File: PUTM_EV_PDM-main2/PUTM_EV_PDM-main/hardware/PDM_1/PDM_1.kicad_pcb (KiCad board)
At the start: 4 copper layers, 55 x 100 mm, 148 parts, among them IC2 BTS722204ESAXUMA1, IC3 BTS722204ESAXUMA1, IC4 BTS722204ESAXUMA1, IC5 BTS722204ESAXUMA1, J1 FTSH-107-01-L-DV-K-A, J2 UPT-08-01-01-L-RA, J5 UPT-02-01-01-X-RA, J6 Conn_01x06, J7 UPT-08-01-01-L-RA, U1 STM32G0C1KCTxN, U2 LD1117S33TR_SOT223, U3 LM2675M-5.0/NOPB, U5 MCP2542FDxMF

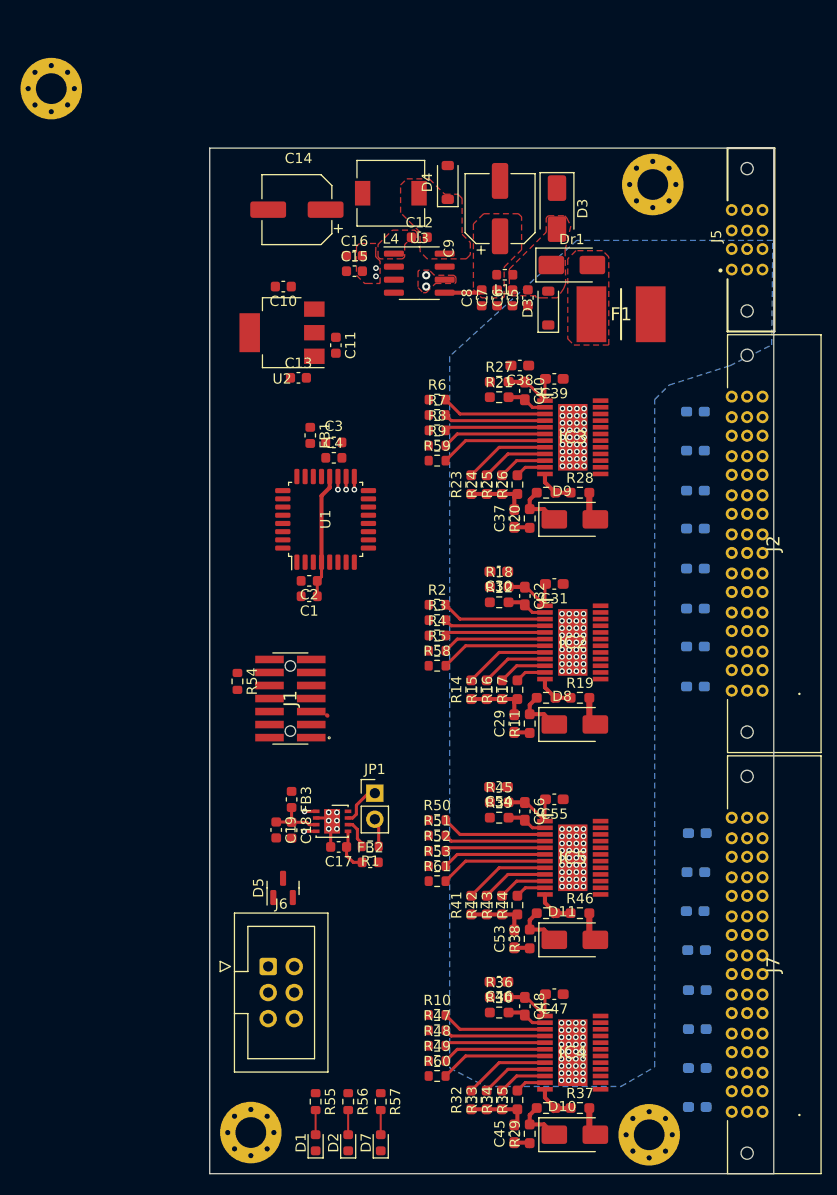
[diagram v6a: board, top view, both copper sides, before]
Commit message: Koniec połączeń sygnałów
Wszystkie sygnały z stm poprowadzone
Zmienione ułożenie połączeń do złącz
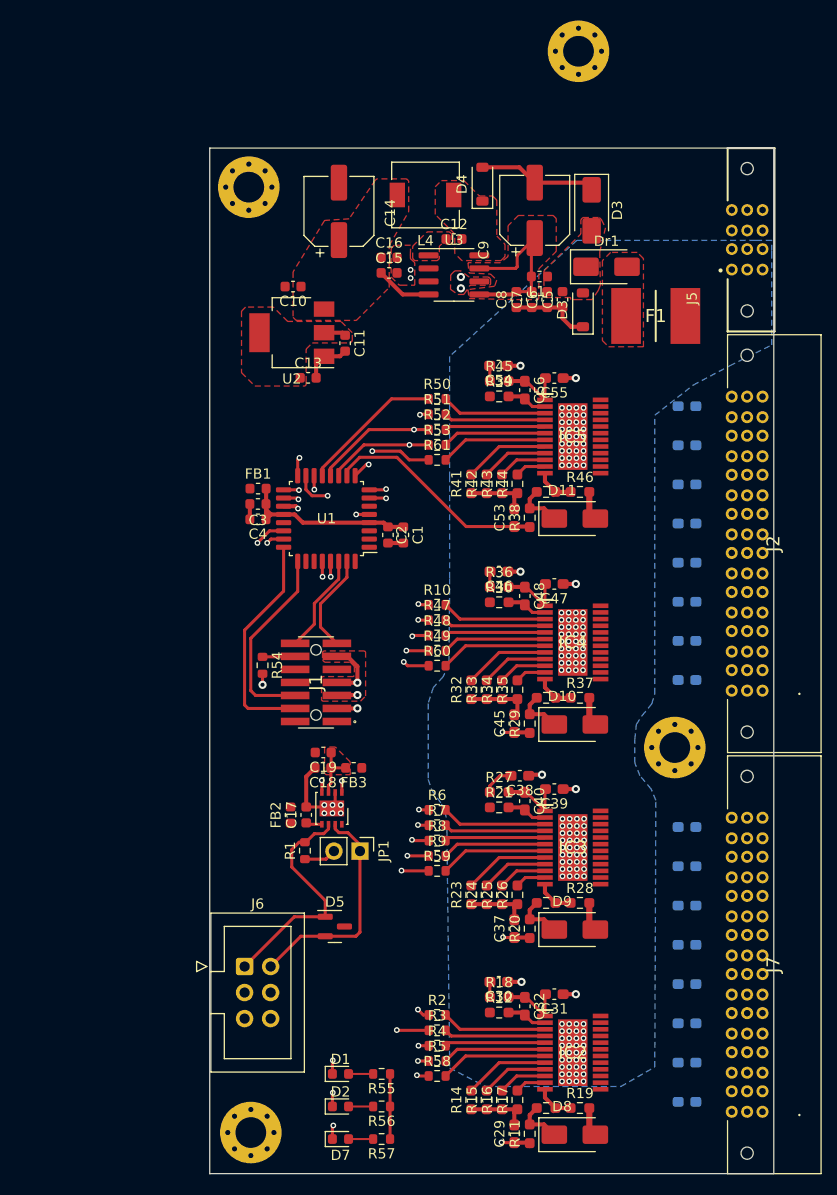
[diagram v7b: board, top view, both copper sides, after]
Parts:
- moved C49 41.7 mm to (171.5, 100.4)
- moved C50 41.7 mm to (171.5, 104.2)
- moved C51 41.7 mm to (171.5, 108.0)
- moved C52 41.6 mm to (171.5, 111.9)
- moved C57 41.6 mm to (171.5, 85.2)
- moved C58 41.6 mm to (171.5, 89.0)
- moved C59 41.6 mm to (171.5, 92.8)
- moved C60 41.6 mm to (171.5, 96.6)
- moved C53 41.1 mm to (154.7, 96.0)
- moved R38 41.1 mm to (156.2, 96.0)
- moved C55 41.1 mm to (158.6, 82.4)
- moved C56 41.1 mm to (155.7, 83.6)
- moved R41 41.1 mm to (150.5, 92.7)
- moved R42 41.1 mm to (152.0, 92.7)
- moved R43 41.1 mm to (153.5, 92.7)
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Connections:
- net /battery connection/IC_1/MISO renamed /battery connection/MISO_1
- net /battery connection/IC_2/MISO renamed /battery connection/MISO_2
- net /battery connection/IC_3/MISO renamed /battery connection/MISO_3
- J2 pad A1: OUT1_0 -> OUT3_3
- J2 pad A2: OUT1_0 -> OUT3_3
- J2 pad A3: OUT1_0 -> OUT3_3
- J2 pad A4: OUT1_0 -> OUT3_3
- J2 pad A5: OUT1_0 -> OUT3_3
- J2 pad A6: OUT1_0 -> OUT3_3
- J2 pad B1: OUT1_1 -> OUT3_2
- J2 pad B2: OUT1_1 -> OUT3_2
- J2 pad B3: OUT1_1 -> OUT3_2
- J2 pad B4: OUT1_1 -> OUT3_2
- J2 pad B5: OUT1_1 -> OUT3_2
- J2 pad B6: OUT1_1 -> OUT3_2
- J2 pad C1: OUT1_2 -> OUT3_1
- J2 pad C2: OUT1_2 -> OUT3_1
- J2 pad C3: OUT1_2 -> OUT3_1
- J2 pad C4: OUT1_2 -> OUT3_1
- J2 pad C5: OUT1_2 -> OUT3_1
- J2 pad C6: OUT1_2 -> OUT3_1
- J2 pad D1: OUT1_3 -> OUT3_0
- J2 pad D2: OUT1_3 -> OUT3_0
- J2 pad D3: OUT1_3 -> OUT3_0
- J2 pad D4: OUT1_3 -> OUT3_0
- J2 pad D5: OUT1_3 -> OUT3_0
- J2 pad D6: OUT1_3 -> OUT3_0
- J2 pad E1: OUT2_0 -> OUT4_3
- J2 pad E2: OUT2_0 -> OUT4_3
- J2 pad E3: OUT2_0 -> OUT4_3
- J2 pad E4: OUT2_0 -> OUT4_3
- J2 pad E5: OUT2_0 -> OUT4_3
- J2 pad E6: OUT2_0 -> OUT4_3
- J2 pad F1: OUT2_1 -> OUT4_2
- J2 pad F2: OUT2_1 -> OUT4_2
- J2 pad F3: OUT2_1 -> OUT4_2
- J2 pad F4: OUT2_1 -> OUT4_2
- J2 pad F5: OUT2_1 -> OUT4_2
- J2 pad F6: OUT2_1 -> OUT4_2
- J2 pad G1: OUT2_2 -> GND
- J2 pad G2: OUT2_2 -> GND
- J2 pad G3: OUT2_2 -> GND
- J2 pad G4: OUT2_2 -> GND
- J2 pad G5: OUT2_2 -> GND
- J2 pad G6: OUT2_2 -> GND
- J2 pad H1: OUT2_3 -> GND
- J2 pad H2: OUT2_3 -> GND
- J2 pad H3: OUT2_3 -> GND
- J2 pad H4: OUT2_3 -> GND
- J2 pad H5: OUT2_3 -> GND
- J2 pad H6: OUT2_3 -> GND
- J5 pad P01_1: (no net) -> +BATT
- J5 pad P01_2: (no net) -> +BATT
- J5 pad P01_3: (no net) -> +BATT
- J5 pad P01_4: (no net) -> +BATT
- J5 pad P01_5: (no net) -> +BATT
- J5 pad P01_6: (no net) -> +BATT
- J5 pad P02_1: (no net) -> GND
- J5 pad P02_2: (no net) -> GND
- J5 pad P02_3: (no net) -> GND
- J5 pad P02_4: (no net) -> GND
- J5 pad P02_5: (no net) -> GND
- J5 pad P02_6: (no net) -> GND
- J7 pad B1: OUT3_0 -> OUT1_2
- J7 pad B2: OUT3_0 -> OUT1_2
- J7 pad B3: OUT3_0 -> OUT1_2
- J7 pad B4: OUT3_0 -> OUT1_2
- J7 pad B5: OUT3_0 -> OUT1_2
- J7 pad B6: OUT3_0 -> OUT1_2
- J7 pad C1: OUT3_1 -> OUT1_1
- J7 pad C2: OUT3_1 -> OUT1_1
- J7 pad C3: OUT3_1 -> OUT1_1
- J7 pad C4: OUT3_1 -> OUT1_1
- J7 pad C5: OUT3_1 -> OUT1_1
- J7 pad C6: OUT3_1 -> OUT1_1
- J7 pad D1: OUT3_2 -> OUT1_0
- J7 pad D2: OUT3_2 -> OUT1_0
- J7 pad D3: OUT3_2 -> OUT1_0
- J7 pad D4: OUT3_2 -> OUT1_0
- J7 pad D5: OUT3_2 -> OUT1_0
- J7 pad D6: OUT3_2 -> OUT1_0
- J7 pad E1: OUT3_3 -> OUT2_3
- J7 pad E2: OUT3_3 -> OUT2_3
- J7 pad E3: OUT3_3 -> OUT2_3
- J7 pad E4: OUT3_3 -> OUT2_3
- J7 pad E5: OUT3_3 -> OUT2_3
- J7 pad E6: OUT3_3 -> OUT2_3
- J7 pad F1: OUT4_0 -> OUT2_2
- J7 pad F2: OUT4_0 -> OUT2_2
- J7 pad F3: OUT4_0 -> OUT2_2
- J7 pad F4: OUT4_0 -> OUT2_2
- J7 pad F5: OUT4_0 -> OUT2_2
- J7 pad F6: OUT4_0 -> OUT2_2
- J7 pad G1: OUT4_1 -> OUT2_1
- J7 pad G2: OUT4_1 -> OUT2_1
- J7 pad G3: OUT4_1 -> OUT2_1
- J7 pad G4: OUT4_1 -> OUT2_1
- J7 pad G5: OUT4_1 -> OUT2_1
- J7 pad G6: OUT4_1 -> OUT2_1
- J7 pad H1: OUT4_2 -> OUT2_0
- J7 pad H2: OUT4_2 -> OUT2_0
- J7 pad H3: OUT4_2 -> OUT2_0
- J7 pad H4: OUT4_2 -> OUT2_0
- J7 pad H5: OUT4_2 -> OUT2_0
- J7 pad H6: OUT4_2 -> OUT2_0
- R54 pad 2: +3V3 -> +3.3V
- U1 pad 26: /CAN_RXD -> unconnected-(U1-PD0-Pad26)
- U1 pad 27: /CAN_TXD -> unconnected-(U1-PD1-Pad27)
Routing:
- net /SPI1_SCK: track 0.00 -> 77.0 mm, vias 0 -> 4
- net /SPI1_NSS: track 0.00 -> 76.8 mm, vias 0 -> 4
- net /FUSE1_IS: track 1.59 -> 74.1 mm, vias 0 -> 2
- net /LED3: track 1.27 -> 70.4 mm, vias 1 -> 2
- net /LED2: track 1.27 -> 65.9 mm, vias 1 -> 2
- net /SPI1_MOSI: track 0.00 -> 60.5 mm, vias 0 -> 2
- net /LED1: track 1.27 -> 61.4 mm, vias 1 -> 2
- net /LHI_1: track 0.00 -> 55.2 mm, vias 0 -> 2
- net /FUSE2_IS: track 1.59 -> 54.8 mm, vias 0 -> 2
- net GND: track 40.3 -> 88.4 mm, vias 10 -> 13
- net /FUSE3_IS: track 1.59 -> 38.1 mm, vias 0 -> 2
- net /LHI_2: track 0.00 -> 35.7 mm, vias 0 -> 2
- net /CAN_RXD: track 0.99 -> 29.8 mm, vias 1 -> 2
- net /CAN_TXD: track 0.94 -> 29.1 mm, vias 1 -> 2
- net /LHI_3: track 0.00 -> 25.6 mm, vias 0 -> 2
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- added copper zone on F.Cu, net +3.3V
- added copper zone on F.Cu, net +5V
- added copper zone on F.Cu, net /CAN/CAN_VDD

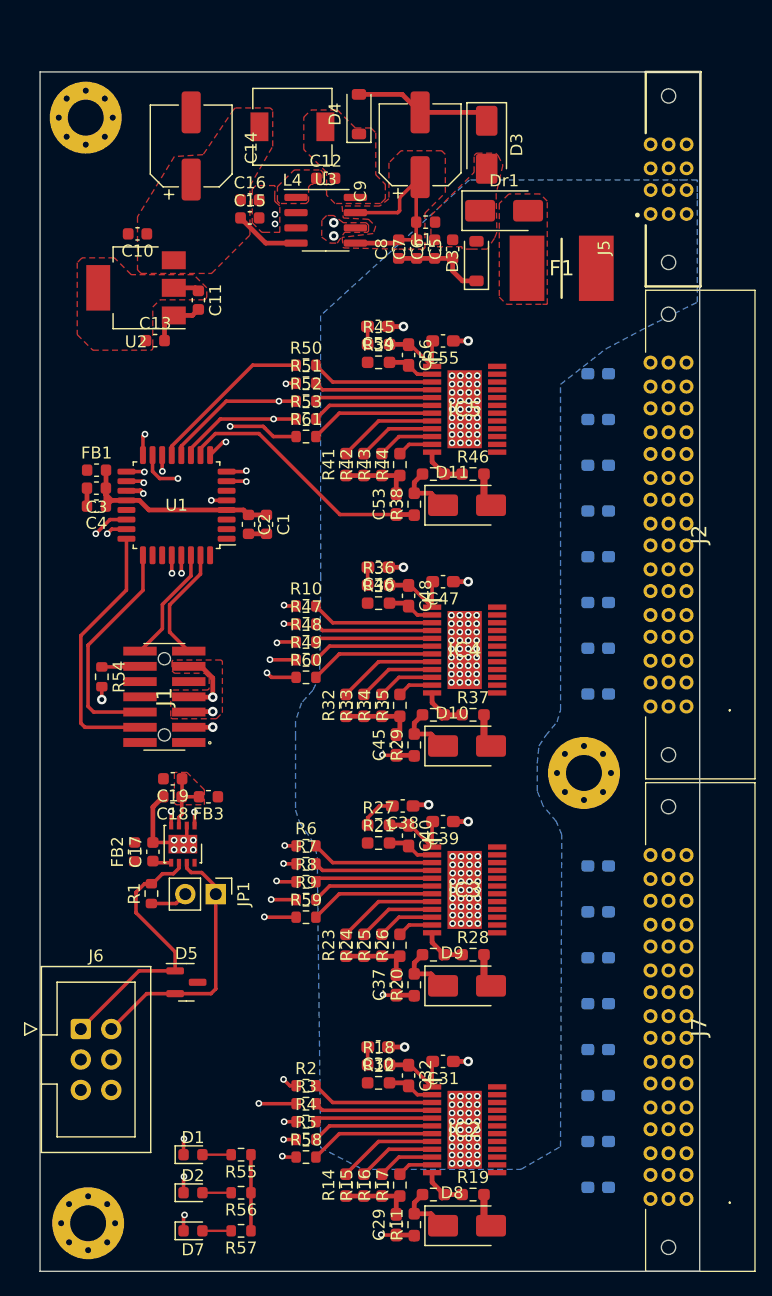
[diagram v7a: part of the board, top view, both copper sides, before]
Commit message: Nowe połączenia
dodana warstwa gnd
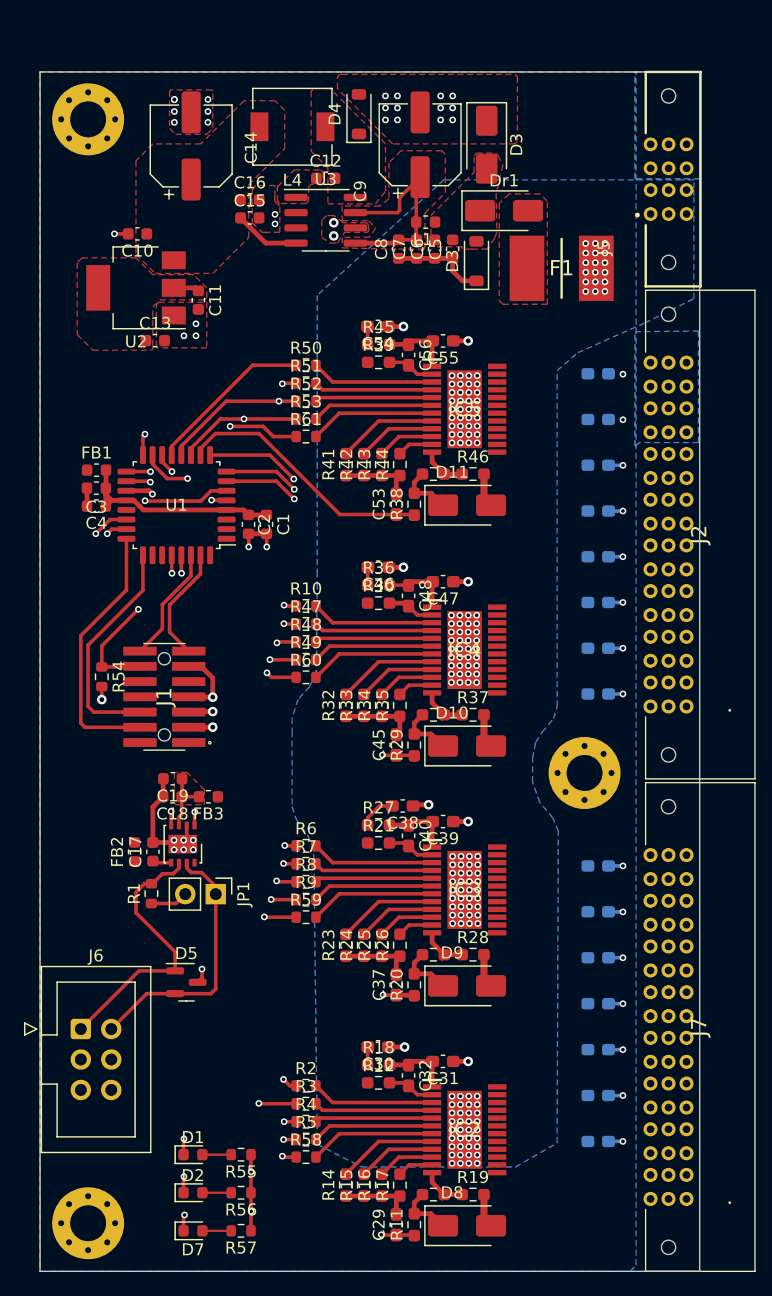
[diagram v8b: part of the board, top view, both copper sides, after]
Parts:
- removed C36: 10n, Capacitor_SMD:C_0603_1608Metric_Pad1.08x0.95mm_HandSolder
- moved REF** 0.24 mm to (129.0, 64.0)
- moved REF** 0.05 mm to (170.4, 118.5)
- turned C33 to 180 degrees
- turned C34 to 180 degrees
- turned C35 to 180 degrees
- turned C41 to 180 degrees
- turned C42 to 180 degrees
- turned C43 to 180 degrees
- turned C44 to 180 degrees
- turned C49 to 180 degrees
- turned C50 to 180 degrees
- turned C51 to 180 degrees
- turned C52 to 180 degrees
- turned C57 to 180 degrees
- turned C58 to 180 degrees
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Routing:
- net /NRST: track 3.20 -> 25.8 mm, vias 0 -> 2
- net GND: track 88.4 -> 78.3 mm, vias 13 -> 39
- net /FUSE3_IS: track 38.1 -> 36.6 mm
- net OUT4_2: track 0.00 -> 1.20 mm, vias 0 -> 1
- net OUT1_0: track 0.00 -> 1.20 mm, vias 0 -> 1
- net OUT3_1: track 0.00 -> 1.20 mm, vias 0 -> 1
- net OUT3_3: track 0.00 -> 1.20 mm, vias 0 -> 1
- net OUT2_3: track 0.00 -> 1.20 mm, vias 0 -> 1
- net OUT2_2: track 0.00 -> 1.20 mm, vias 0 -> 1
- net OUT4_3: track 0.00 -> 1.20 mm, vias 0 -> 1
- net OUT1_1: track 0.00 -> 1.20 mm, vias 0 -> 1
- net OUT3_0: track 0.00 -> 1.20 mm, vias 0 -> 1
- net OUT2_1: track 0.00 -> 1.20 mm, vias 0 -> 1
- net OUT1_2: track 0.00 -> 1.20 mm, vias 0 -> 1
- net OUT3_2: track 0.00 -> 1.20 mm, vias 0 -> 1
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- added copper zone on B.Cu, net GND
